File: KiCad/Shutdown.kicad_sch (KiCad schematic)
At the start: 35 parts, among them Q1 SQ2308CES, Q2 DMPH6050SSDQ-13, Q3 SQ2308CES, U1 SN74HCS08, U2 LTC6993HS6-2, U3 74LVC2G32, U4 74LVC2G08, U5 SN74LVC74AQPW, U6 MIC4127YMME

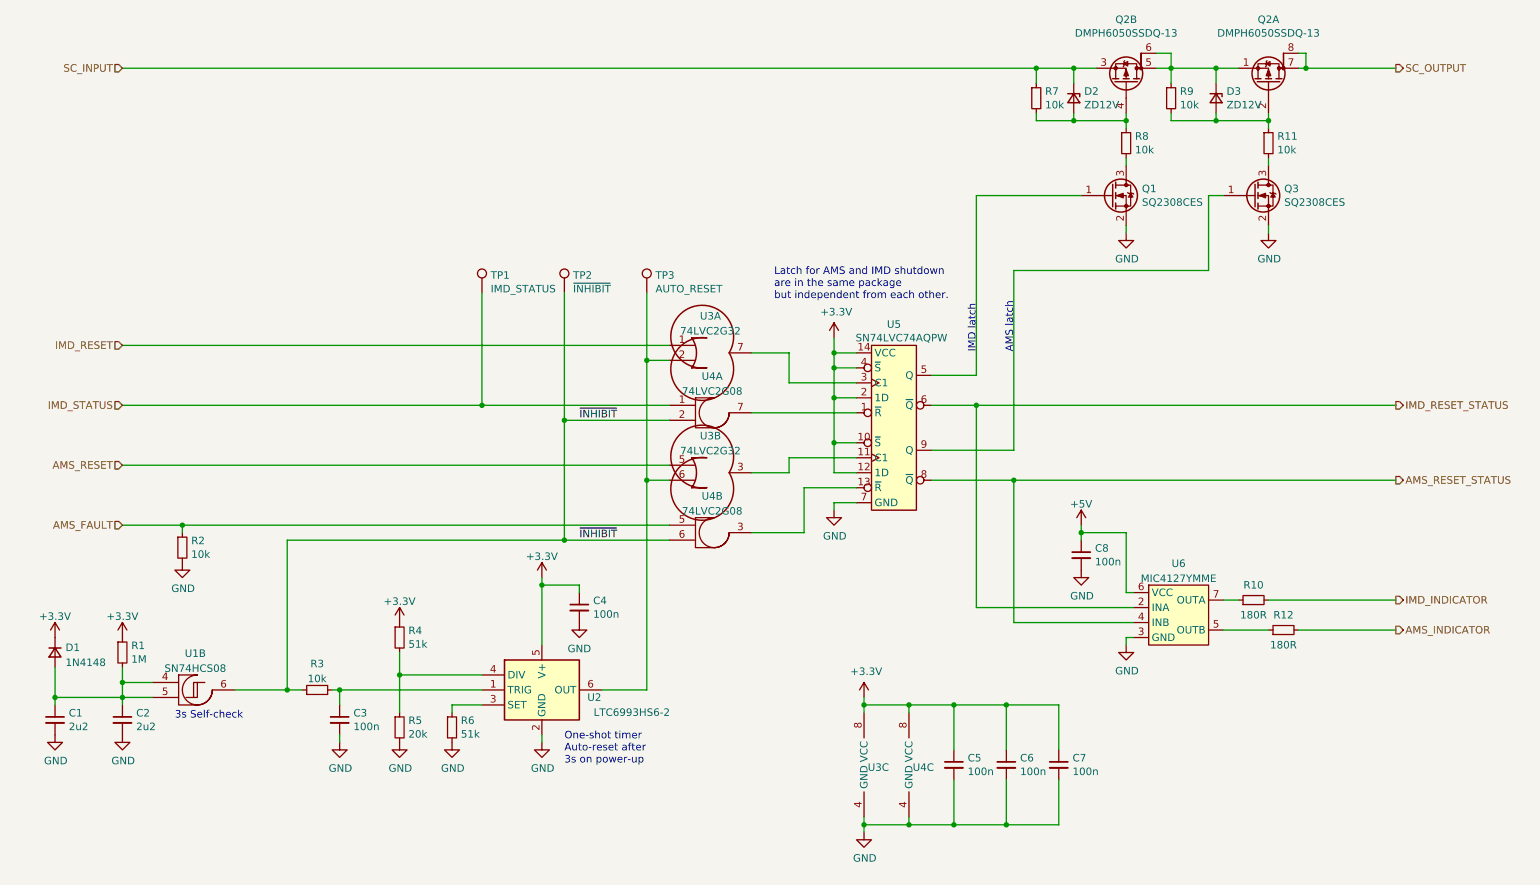
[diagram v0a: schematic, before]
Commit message: Port to Kicad 7, small changes in auto-reset feature
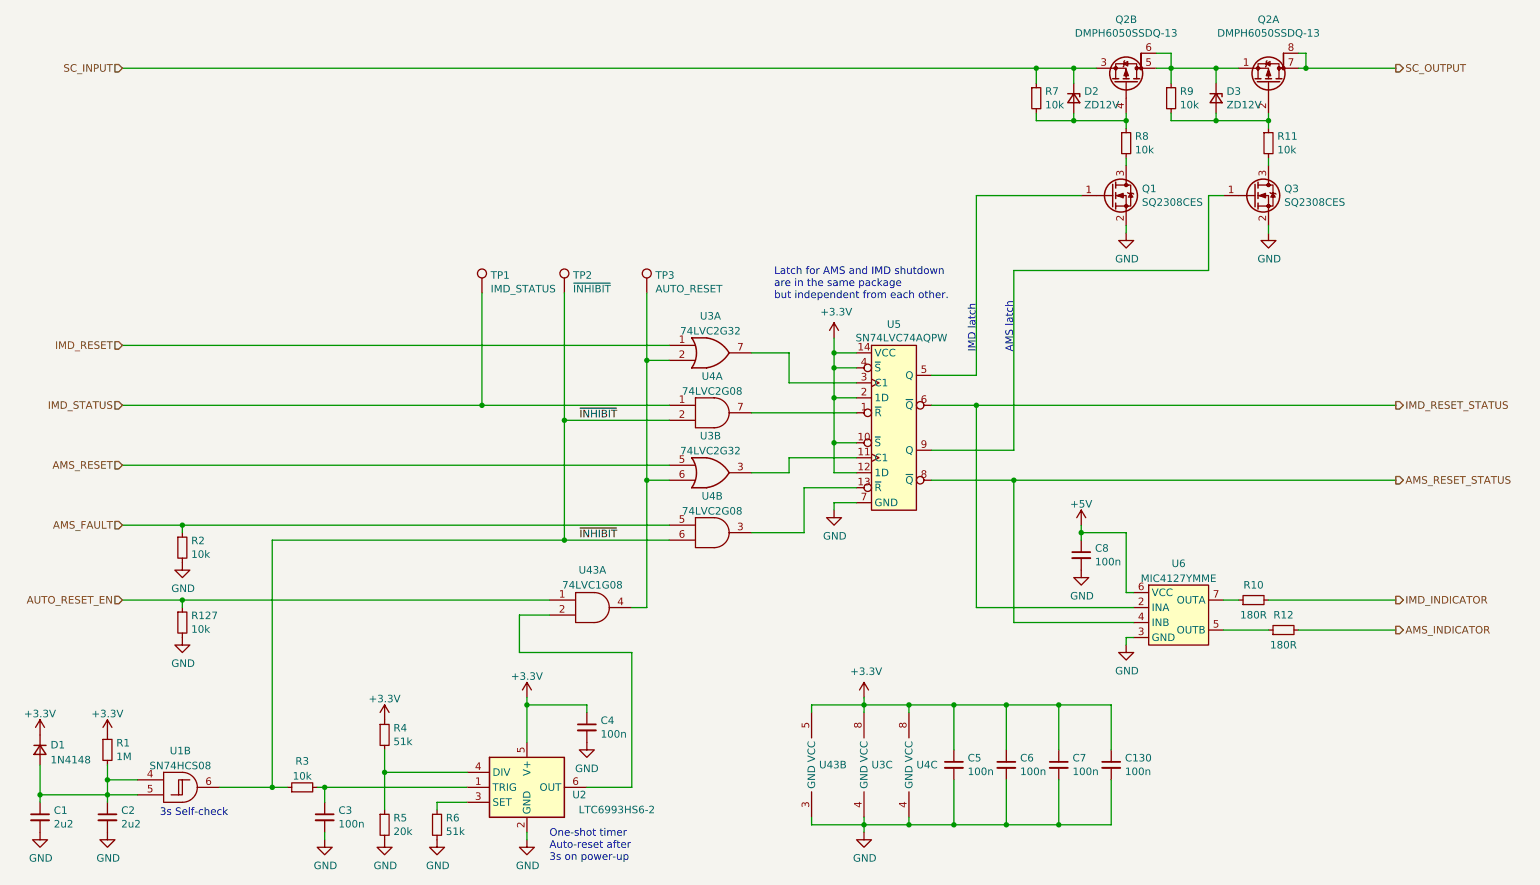
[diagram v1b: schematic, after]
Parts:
- added C130: 100n, Capacitor_SMD:C_0603_1608Metric, symbol Device:C_Small
- added R127: 10k, Resistor_SMD:R_0603_1608Metric, symbol Device:R_Small
- added U43: 74LVC1G08, Package_TO_SOT_SMD:SOT-23-5, symbol Scuderia:74xx1G08
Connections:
- net +3.3V: now also C130.1, U43.5 (VCC)
- net GND: now also C130.2, R127.2, U43.3 (GND)
- net at TP3.1, U3.2, U3.6: now also U43.4; no longer U2.6 (OUT)
- new net: U2.6 (OUT), U43.2
- new net AUTO_RESET_EN: R127.1, U43.1
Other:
- moved on the sheet: C1, C2, C3, C4, D1, R1, R3, R4, R5, R6, U1B, U2
